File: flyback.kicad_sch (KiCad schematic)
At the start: 16 parts, among them Q1 IPD050N10N5, Q2 IPD050N10N5, T1 MSD1514-103ME

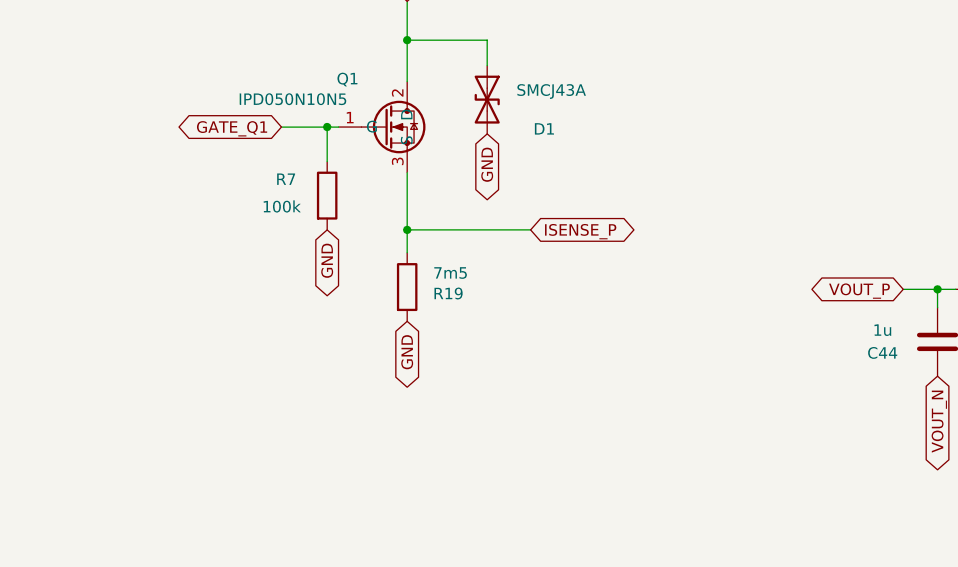
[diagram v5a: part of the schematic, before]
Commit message: R19 passe à 10mOhm, Yageo WSK1206R0100FEA 4 broches Kelvin
Remplace le 7,5mOhm/1210/2 broches par le shunt Kelvin sourcé par
l'utilisateur. Pastilles 2/4 (force) reprennent exactement la position
des pins de l'ancien Device:R -- aucun fil/label existant du chemin
ISENSE_P/GND à retoucher. Pastilles 1/3 (sense, mapping confirmé par
l'utilisateur) exposées en nouveaux labels ISNS_KP/ISNS_KN, consommés
par la future feuille limitation-courant.

Co-Authored-By: Claude Sonnet 5 <noreply@anthropic.com>
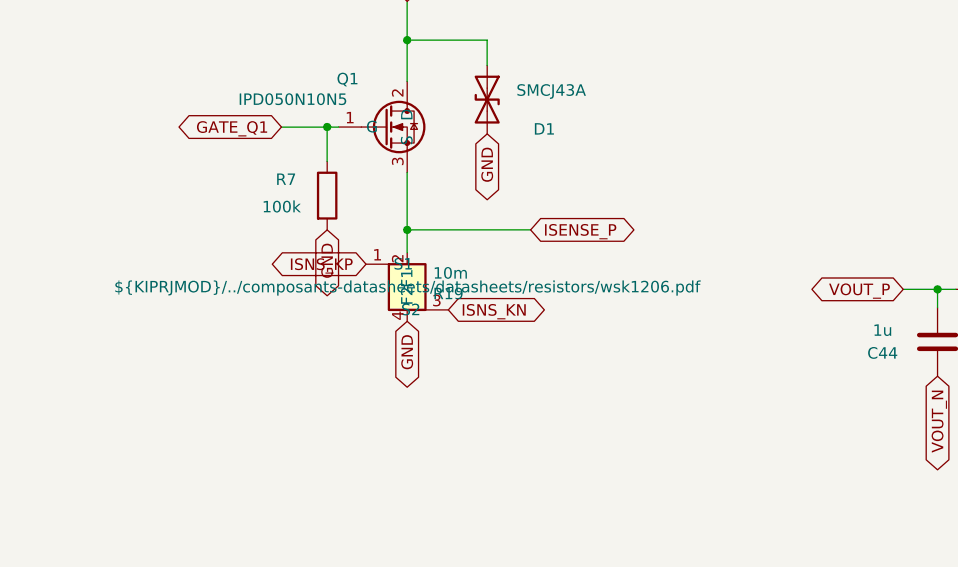
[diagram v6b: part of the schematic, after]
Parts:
- R19: value 7m5 -> 10m; footprint Resistor_SMD:R_1210_3225Metric -> WSK1206:WSK1206R0100FEA; symbol Device:R -> custom_parts:WSK1206R0100FEA
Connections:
- net GND: now also R19.4 (F2); no longer R19.2
- net ISENSE_P: now also R19.2 (F1); no longer R19.1
- new net ISNS_KN: R19.3 (S2)
- new net ISNS_KP: R19.1 (S1)
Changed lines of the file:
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@@
+		)
+	)
+	(global_label "ISNS_KP"
+		(shape bidirectional)
+		(at 75.438 86.36 180)
+		(fields_autoplaced yes)
+		(effects
+			(font
+				(size 1.27 1.27)
+			)
+			(justify right)
+		)
+		(property "Intersheetrefs" "${INTERSHEET_REFS}"
+			(at 75.438 86.36 0)
+			(hide yes)
+			(show_name no)
+			(do_not_autoplace no)
+			(effects
+				(font
+					(size 1.27 1.27)
+				)
+			)
+		)
+	)
+	(global_label "ISNS_KN"
+		(shape bidirectional)
+		(at 84.582 91.44 0)
+		(fields_autoplaced yes)
+		(effects
+			(font
+				(size 1.27 1.27)
+			)
+			(justify left)
+		)
+		(property "Intersheetrefs" "${INTERSHEET_REFS}"
+			(at 84.582 91.44 0)
+			(hide yes)
+			(show_name no)
+			(do_not_autoplace no)
+			(effects
+				(font
+					(size 1.27 1.27)
+				)
+			)
 		)
 	)
@@
 	)
 	(symbol
-		(lib_id "Device:R")
+		(lib_id "custom_parts:WSK1206R0100FEA")
 		(at 80.01 88.9 0)
 		(unit 1)
@@
 			)
 		)
-		(property "Value" "7m5"
+		(property "Value" "10m"
 			(at 84.836 87.376 0)
 			(show_name no)
@@
 			)
 		)
-		(property "Footprint" "Resistor_SMD:R_1210_3225Metric"
+		(property "Footprint" "WSK1206:WSK1206R0100FEA"
 			(at 80.01 88.9 0)
 			(hide yes)
@@
 			)
 		)
-		(property "Datasheet" ""
+		(property "Datasheet" "${KIPRJMOD}/../composants-datasheets/datasheets/resistors/wsk1206.pdf"
 			(at 80.01 88.9 0)
 			(show_name no)
@@
 		(pin "2"
 		)
+		(pin "3"
+		)
+		(pin "4"
+		)
 		(instances

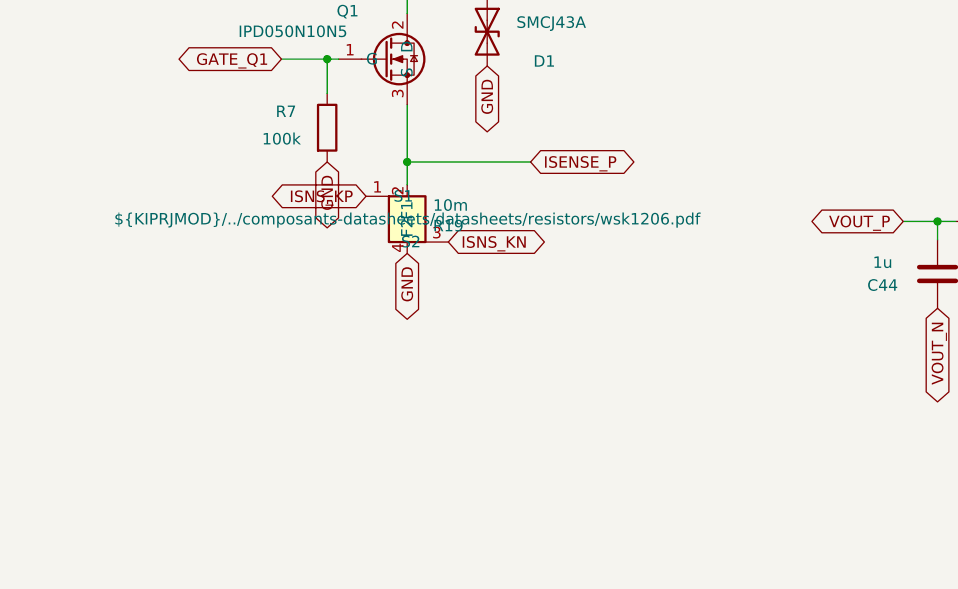
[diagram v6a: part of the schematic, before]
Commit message: Ajoute une LED de defaut sur Q_TRIP (R34/D6), corrige un bug d'insertion lib_symbols
Q_TRIP (sortie de reserve du verrou) recoit un usage reel : LED rouge 3mm
+ 10k, polarite ajustee par l'utilisateur pour s'allumer en defaut latche
(Q_TRIP -> D6 -> R34 -> GND, verifie par export netlist).

Corrige au passage une insertion incorrecte du bloc lib_symbols de
Device:LED (imbrique par erreur dans l'etiquette globale ISNS_AMP au lieu
de suivre la vraie fermeture de lib_symbols), qui empechait le chargement
de la feuille. Documente dans l'addendum du S19.

Co-Authored-By: Claude Sonnet 5 <noreply@anthropic.com>
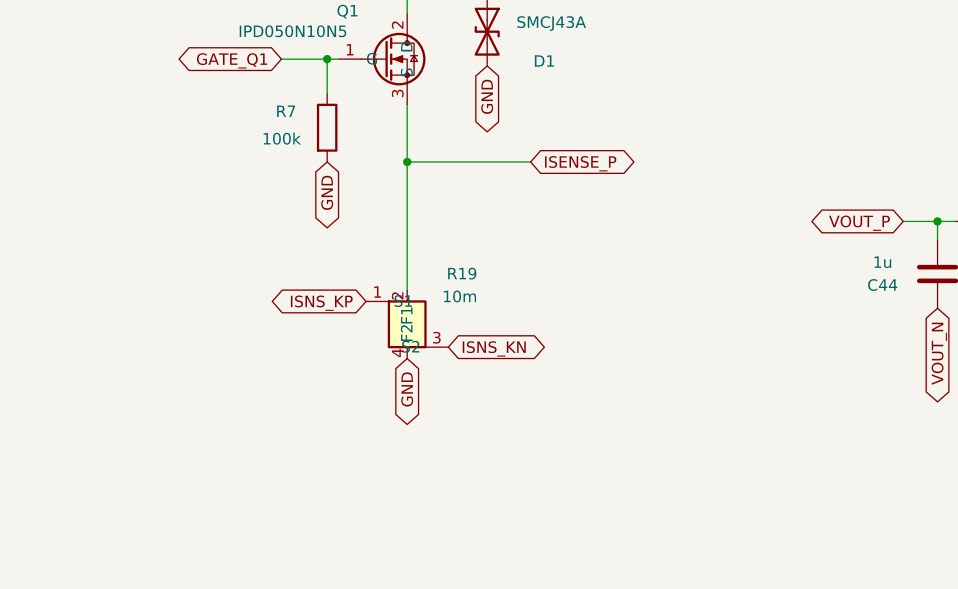
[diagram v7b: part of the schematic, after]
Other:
- moved on the sheet: R19
